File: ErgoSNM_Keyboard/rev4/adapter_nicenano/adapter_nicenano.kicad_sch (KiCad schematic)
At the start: 8 parts, among them J1 Conn_01x13, J2 Conn_01x03, J3 Conn_01x13, J4 Conn_01x30

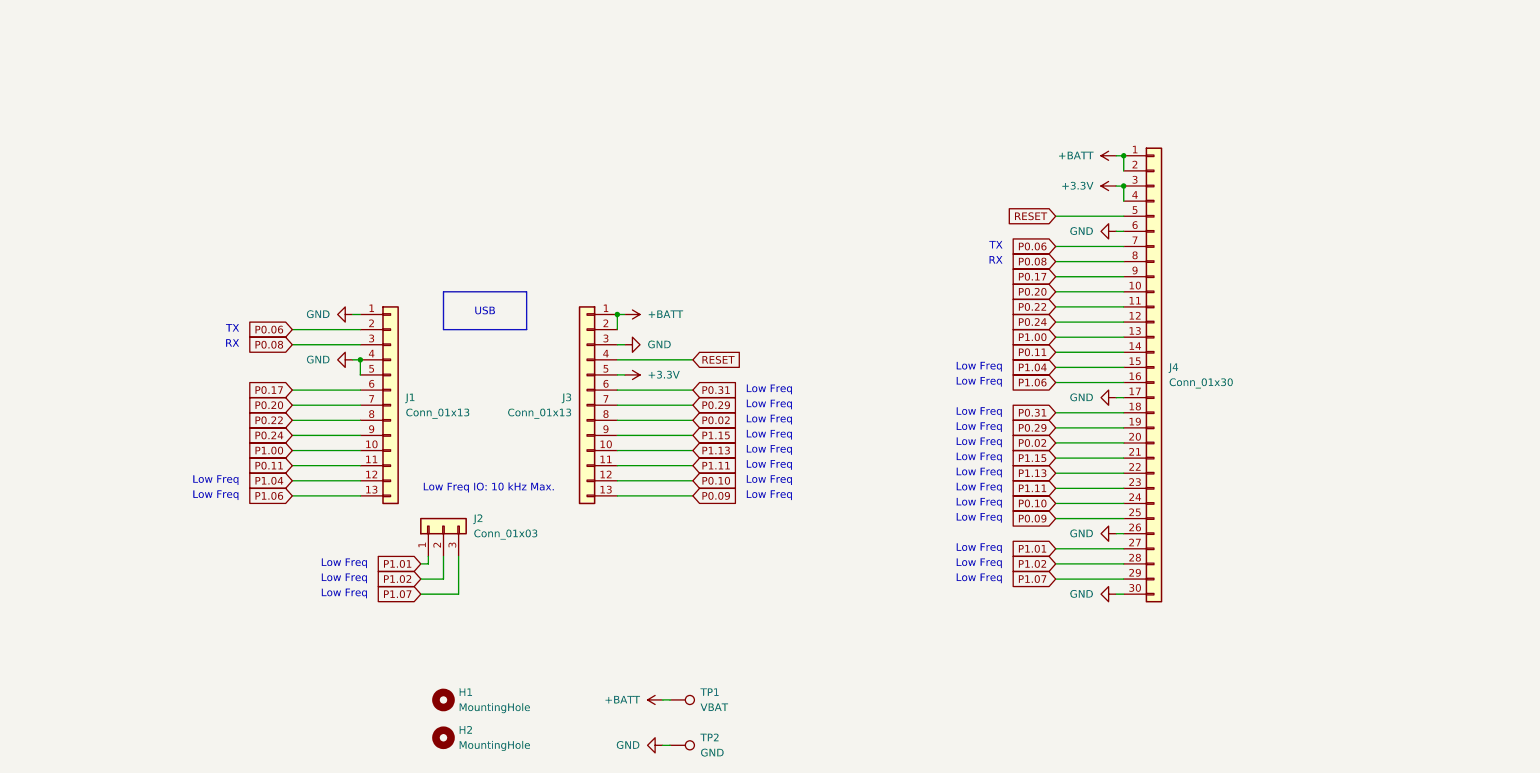
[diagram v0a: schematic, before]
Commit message: feat: add v4 mdbt50q board
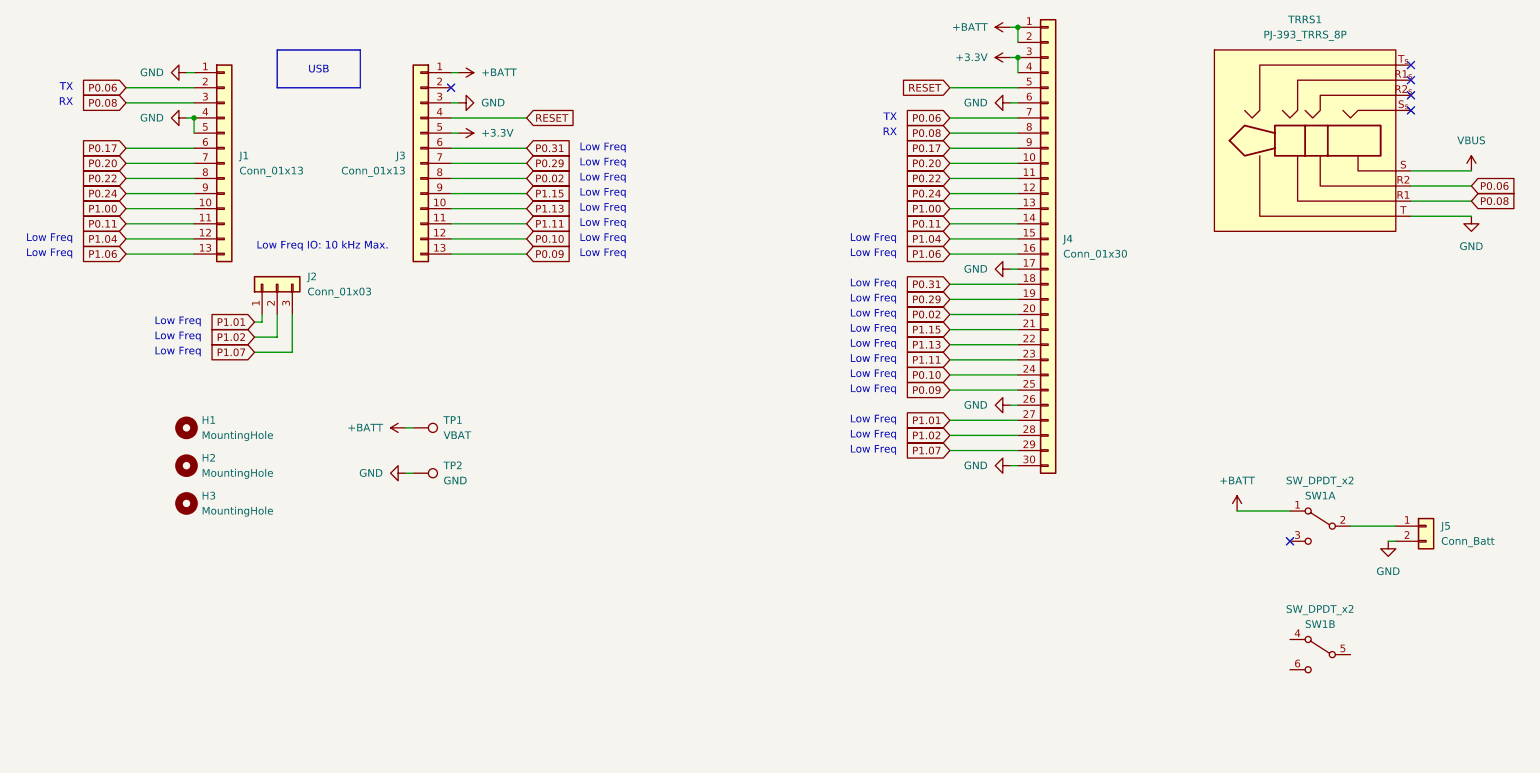
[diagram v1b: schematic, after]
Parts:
- added H3: MountingHole, MountingHole:MountingHole_2.7mm_M2.5_ISO7380, symbol Mechanical:MountingHole
- added J5: Conn_Batt, Connector_JST:JST_PH_S2B-PH-SM4-TB_1x02-1MP_P2.00mm_Horizontal, symbol Connector_Generic:Conn_01x02
- added SW1: SW_DPDT_x2, ErgoSNM_Keyboard:MSKT-22D14-T, symbol Switch:SW_DPDT_x2
- added TRRS1: PJ-393_TRRS_8P, ErgoSNM_Keyboard:PJ-393 8P TRRS, symbol ErgoSNM_Keyboard_Library:PJ-393_TRRS_8P
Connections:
- net +BATT: now also SW1.1 (A); no longer J3.2 (Pin_2)
- net GND: now also J5.2 (Pin_2), TRRS1.T
- net P0.06: now also TRRS1.R2
- net P0.08: now also TRRS1.R1
- new net: J5.1 (Pin_1), SW1.2 (B)
- new net VBUS: TRRS1.S
- no-connect marks 0 -> 6
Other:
- moved on the sheet: H1, H2, J1, J2, J3, J4, TP1, TP2
